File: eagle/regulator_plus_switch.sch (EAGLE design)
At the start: 67 parts, among them IC2 LT1352PA, IC3 DG419DJN, IC4 LT1352PA, Q1 2N3906, Q2 2N3906, T1 2N3904, T2 2N3904

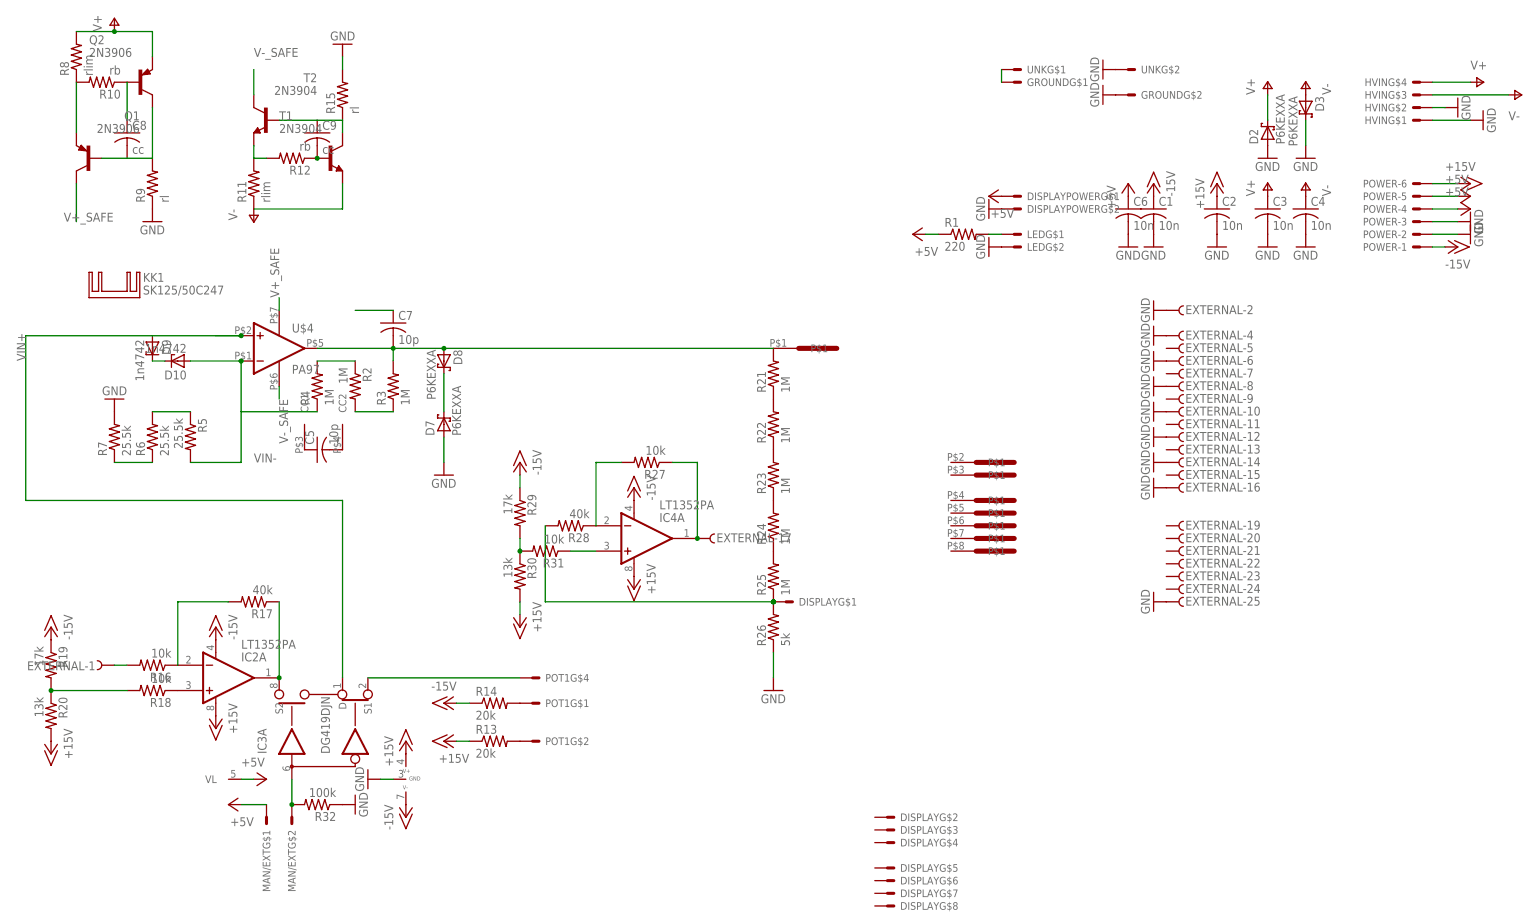
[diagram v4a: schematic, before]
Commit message: overcurrent, worked out connectors
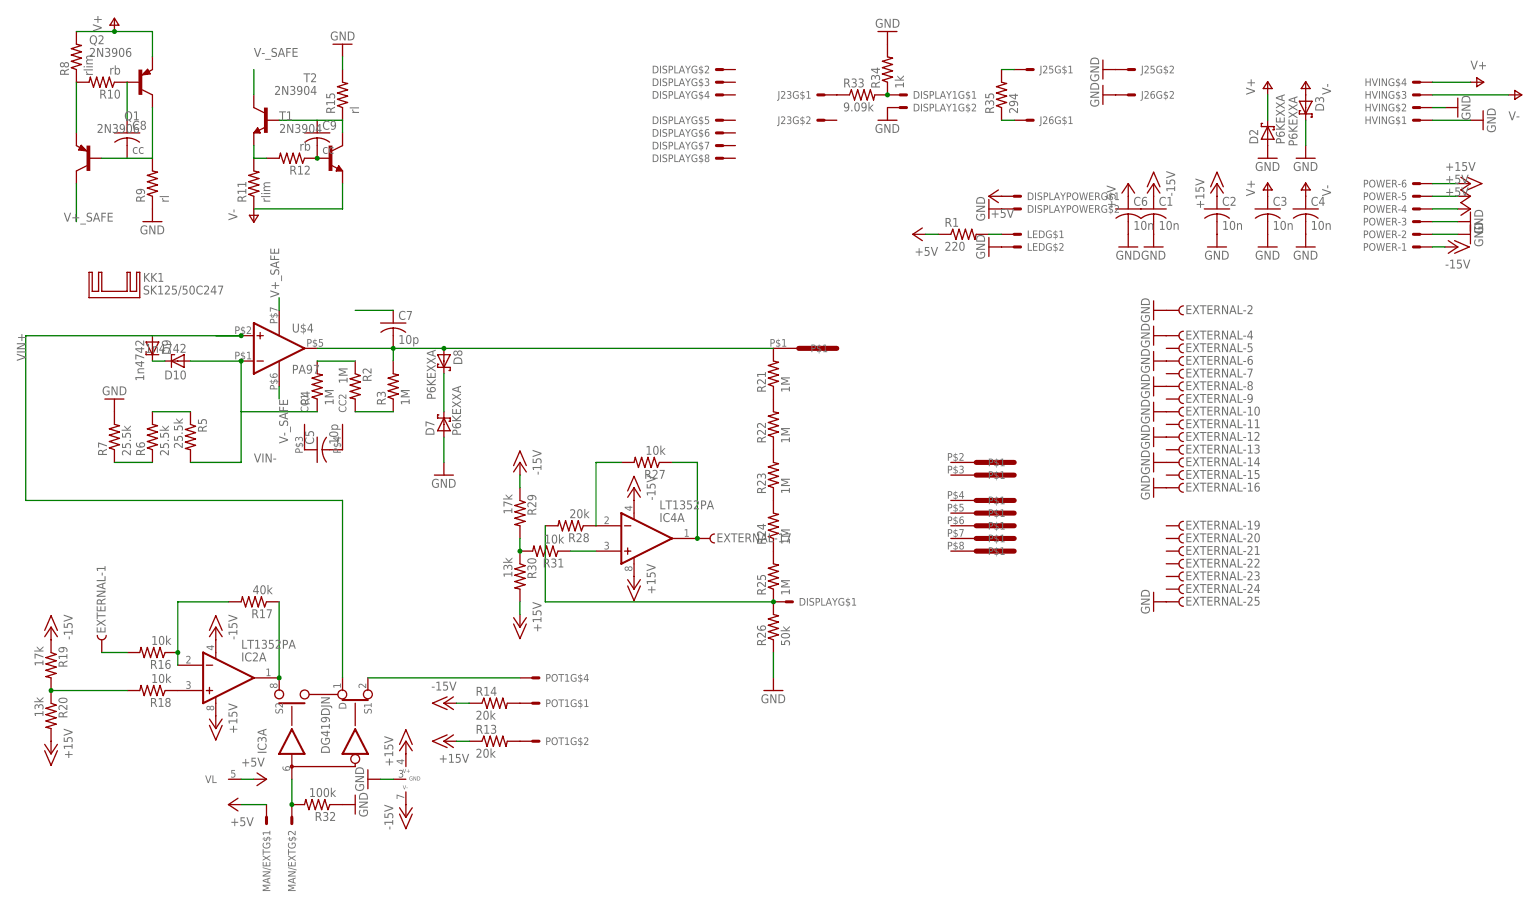
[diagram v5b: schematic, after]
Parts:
- removed GROUND, UNK: 5569-2, con-molex:5569-2
- added DISPLAY1, J23, J25, J26: 5569-2, con-molex:5569-2
- added R33: 9.09k, rcl:R-US_0207/10
- added R34: 1k, rcl:R-US_0207/10
- added R35: 294, rcl:R-US_0207/10
- R26: value 5k -> 50k
- R28: value 40k -> 20k
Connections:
- new net N$20: DISPLAY1G$1.S, R33.2, R34.1
- new net N$21: J23G$1.S, R33.1
- new net N$22: J26G$1.S, R35.1
- net GND: now also DISPLAY1G$2.S, J25G$2.S, J26G$2.S, R34.2; no longer GROUNDG$2.S, UNKG$2.S
- net N$6: now also J25G$1.S, R35.2; no longer GROUNDG$1.S, UNKG$1.S
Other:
- moved on the sheet: DISPLAYG$1, DISPLAYG$2, DISPLAYG$3, DISPLAYG$4, DISPLAYG$5, DISPLAYG$6, DISPLAYG$7, DISPLAYG$8, EXTERNAL-1, R16
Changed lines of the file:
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@@
 <part name="R24" library="resistor" deviceset="R-US_" device="0207/10" value="1M"/>
 <part name="R25" library="resistor" deviceset="R-US_" device="0207/10" value="1M"/>
-<part name="R26" library="rcl" deviceset="R-US_" device="0207/10" value="5k"/>
+<part name="R26" library="rcl" deviceset="R-US_" device="0207/10" value="50k"/>
 <part name="GND24" library="supply1" deviceset="GND" device=""/>
 <part name="IC4" library="linear-technology" deviceset="LT1352" device="PA"/>
@@
 <part name="P+16" library="supply1" deviceset="+15V" device=""/>
 <part name="R27" library="rcl" deviceset="R-US_" device="0207/10" value="10k"/>
-<part name="R28" library="rcl" deviceset="R-US_" device="0207/10" value="40k"/>
+<part name="R28" library="rcl" deviceset="R-US_" device="0207/10" value="20k"/>
 <part name="R29" library="rcl" deviceset="R-US_" device="0207/10" value="17k"/>
 <part name="R30" library="rcl" deviceset="R-US_" device="0207/10" value="13k"/>
@@
 <part name="OUT" library="con-amp-te" deviceset="640584-1" device=""/>
 <part name="DISPLAY" library="con-molex" deviceset="5669-8" device=""/>
-<part name="UNK" library="con-molex" deviceset="5569-2" device=""/>
-<part name="GROUND" library="con-molex" deviceset="5569-2" device=""/>
+<part name="J25" library="con-molex" deviceset="5569-2" device=""/>
+<part name="J26" library="con-molex" deviceset="5569-2" device=""/>
 <part name="DISPLAYPOWER" library="con-molex" deviceset="5569-2" device=""/>
 <part name="LED" library="con-molex" deviceset="5569-2" device=""/>
@@
 <part name="R15" library="rcl" deviceset="R-US_" device="0207/10" value="rl"/>
 <part name="GND31" library="supply1" deviceset="GND" device=""/>
+<part name="DISPLAY1" library="con-molex" deviceset="5569-2" device=""/>
+<part name="R33" library="rcl" deviceset="R-US_" device="0207/10" value="9.09k"/>
+<part name="R34" library="rcl" deviceset="R-US_" device="0207/10" value="1k"/>
+<part name="GND32" library="supply1" deviceset="GND" device=""/>
+<part name="GND33" library="supply1" deviceset="GND" device=""/>
+<part name="J23" library="con-molex" deviceset="5569-2" device=""/>
+<part name="R35" library="rcl" deviceset="R-US_" device="0207/10" value="294"/>
 </parts>
 <sheets>
@@
 <instance part="HVIN" gate="G$4" x="294.64" y="840.74" rot="R180"/>
 <instance part="IC2" gate="A" x="55.88" y="721.36" rot="MR180"/>
-<instance part="R16" gate="G$1" x="40.64" y="723.9" rot="R180"/>
+<instance part="R16" gate="G$1" x="40.64" y="726.44" rot="R180"/>
 <instance part="R17" gate="G$1" x="60.96" y="736.6" rot="R180"/>
 <instance part="R18" gate="G$1" x="40.64" y="718.82" rot="R180"/>
@@
 <instance part="P-5" gate="1" x="91.44" y="693.42"/>
 <instance part="GND12" gate="1" x="83.82" y="701.04" rot="R270"/>
-<instance part="EXTERNAL" gate="-1" x="30.48" y="723.9" rot="R180"/>
+<instance part="EXTERNAL" gate="-1" x="30.48" y="728.98" rot="R90"/>
 <instance part="EXTERNAL" gate="-2" x="246.38" y="795.02"/>
 <instance part="EXTERNAL" gate="-4" x="246.38" y="789.94"/>
@@
 <instance part="OUT" gate="G$7" x="205.74" y="749.3"/>
 <instance part="OUT" gate="G$8" x="205.74" y="746.76"/>
-<instance part="DISPLAY" gate="G$1" x="167.64" y="736.6"/>
-<instance part="DISPLAY" gate="G$2" x="187.96" y="693.42"/>
-<instance part="DISPLAY" gate="G$3" x="187.96" y="690.88"/>
-<instance part="DISPLAY" gate="G$4" x="187.96" y="688.34"/>
-<instance part="DISPLAY" gate="G$5" x="187.96" y="683.26"/>
-<instance part="DISPLAY" gate="G$6" x="187.96" y="680.72"/>
-<instance part="DISPLAY" gate="G$7" x="187.96" y="678.18"/>
-<instance part="DISPLAY" gate="G$8" x="187.96" y="675.64"/>
-<instance part="UNK" gate="G$1" x="213.36" y="843.28"/>
-<instance part="UNK" gate="G$2" x="236.22" y="843.28"/>
-<instance part="GROUND" gate="G$1" x="213.36" y="840.74"/>
-<instance part="GROUND" gate="G$2" x="236.22" y="838.2"/>
+<instance part="DISPLAY" gate="G$1" x="167.64" y="736.6" rot="MR180"/>
+<instance part="DISPLAY" gate="G$2" x="154.94" y="843.28" rot="MR0"/>
+<instance part="DISPLAY" gate="G$3" x="154.94" y="840.74" rot="MR0"/>
+<instance part="DISPLAY" gate="G$4" x="154.94" y="838.2" rot="MR0"/>
+<instance part="DISPLAY" gate="G$5" x="154.94" y="833.12" rot="MR0"/>
+<instance part="DISPLAY" gate="G$6" x="154.94" y="830.58" rot="MR0"/>
+<instance part="DISPLAY" gate="G$7" x="154.94" y="828.04" rot="MR0"/>
+<instance part="DISPLAY" gate="G$8" x="154.94" y="825.5" rot="MR0"/>
+<instance part="J25" gate="G$1" x="215.9" y="843.28"/>
+<instance part="J25" gate="G$2" x="236.22" y="843.28"/>
+<instance part="J26" gate="G$1" x="215.9" y="833.12"/>
+<instance part="J26" gate="G$2" x="236.22" y="838.2"/>
 <instance part="DISPLAYPOWER" gate="G$1" x="213.36" y="817.88"/>
 <instance part="DISPLAYPOWER" gate="G$2" x="213.36" y="815.34"/>
@@
 <instance part="R15" gate="G$1" x="78.74" y="838.2" rot="R90"/>
 <instance part="GND31" gate="1" x="78.74" y="848.36" rot="R180"/>
+<instance part="DISPLAY1" gate="G$1" x="190.5" y="838.2"/>
+<instance part="DISPLAY1" gate="G$2" x="190.5" y="835.66"/>
+<instance part="R33" gate="G$1" x="182.88" y="838.2"/>
+<instance part="R34" gate="G$1" x="187.96" y="843.28" rot="R90"/>
+<instance part="GND32" gate="1" x="187.96" y="850.9" rot="R180"/>
+<instance part="GND33" gate="1" x="187.96" y="833.12"/>
+<instance part="J23" gate="G$1" x="175.26" y="838.2" rot="R180"/>
+<instance part="J23" gate="G$2" x="175.26" y="833.12" rot="R180"/>
+<instance part="R35" gate="G$1" x="210.82" y="838.2" rot="R90"/>
 </instances>
 <busses>
@@
 </segment>
 <segment>
-<pinref part="UNK" gate="G$2" pin="S"/>
+<pinref part="J25" gate="G$2" pin="S"/>
 <pinref part="GND7" gate="1" pin="GND"/>
 </segment>
 <segment>
-<pinref part="GROUND" gate="G$2" pin="S"/>
+<pinref part="J26" gate="G$2" pin="S"/>
 <pinref part="GND8" gate="1" pin="GND"/>
 </segment>
@@
 <pinref part="GND31" gate="1" pin="GND"/>
 <wire x1="78.74" y1="843.28" x2="78.74" y2="845.82" width="0.1524" layer="91"/>
+</segment>
+<segment>
+<pinref part="R34" gate="G$1" pin="2"/>
+<pinref part="GND32" gate="1" pin="GND"/>
+</segment>
+<segment>
+<pinref part="DISPLAY1" gate="G$2" pin="S"/>
+<pinref part="GND33" gate="1" pin="GND"/>
 </segment>
 </net>
@@
 <pinref part="R17" gate="G$1" pin="2"/>
 <wire x1="55.88" y1="736.6" x2="45.72" y2="736.6" width="0.1524" layer="91"/>
-<wire x1="45.72" y1="736.6" x2="45.72" y2="723.9" width="0.1524" layer="91"/>
+<wire x1="45.72" y1="736.6" x2="45.72" y2="726.44" width="0.1524" layer="91"/>
+<wire x1="45.72" y1="726.44" x2="45.72" y2="723.9" width="0.1524" layer="91"/>
+<junction x="45.72" y="726.44"/>
 </segment>
 </net>
@@
 <pinref part="R16" gate="G$1" pin="2"/>
 <pinref part="EXTERNAL" gate="-1" pin="F"/>
-<wire x1="33.02" y1="723.9" x2="35.56" y2="723.9" width="0.1524" layer="91"/>
+<wire x1="30.48" y1="726.44" x2="35.56" y2="726.44" width="0.1524" layer="91"/>
 </segment>
 </net>
@@
 <wire x1="165.1" y1="736.6" x2="119.38" y2="736.6" width="0.1524" layer="91"/>
 <wire x1="119.38" y1="736.6" x2="119.38" y2="751.84" width="0.1524" layer="91"/>
+<junction x="165.1" y="736.6"/>
 <pinref part="DISPLAY" gate="G$1" pin="S"/>
-<junction x="165.1" y="736.6"/>
-<junction x="165.1" y="736.6"/>
-<junction x="165.1" y="736.6"/>
 </segment>
 </net>
@@
 <net name="N$6" class="0">
 <segment>
-<pinref part="UNK" gate="G$1" pin="S"/>
-<pinref part="GROUND" gate="G$1" pin="S"/>
-<wire x1="210.82" y1="843.28" x2="210.82" y2="840.74" width="0.1524" layer="91"/>
+<pinref part="J25" gate="G$1" pin="S"/>
+<pinref part="R35" gate="G$1" pin="2"/>
+<wire x1="213.36" y1="843.28" x2="210.82" y2="843.28" width="0.1524" layer="91"/>
 </segment>
 </net>
@@
 </segment>
 </net>
+<net name="N$20" class="0">
+<segment>
+<pinref part="DISPLAY1" gate="G$1" pin="S"/>
+<pinref part="R33" gate="G$1" pin="2"/>
+<pinref part="R34" gate="G$1" pin="1"/>
+<pinref part="R34" gate="G$1" pin="1"/>
+<junction x="187.96" y="838.2"/>
+</segment>
+</net>
+<net name="N$21" class="0">
+<segment>
+<pinref part="R33" gate="G$1" pin="1"/>
+<pinref part="J23" gate="G$1" pin="S"/>
+</segment>
+</net>
+<net name="N$22" class="0">
+<segment>
+<pinref part="J26" gate="G$1" pin="S"/>
+<pinref part="R35" gate="G$1" pin="1"/>
+<wire x1="213.36" y1="833.12" x2="210.82" y2="833.12" width="0.1524" layer="91"/>
+</segment>
+</net>

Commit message: yay led switch worked out
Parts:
- removed DISPLAYPOWER, J25, LED: 5569-2, con-molex:5569-2
- removed R1: 220, rcl:R-US_0207/10
- added DISPLAYPOWERJ25: 5569-2, con-molex:5569-2
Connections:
- removed net N$6: J25G$1.S, R35.2
- removed net N$7: LEDG$1.S, R1.2
- net +5V: now also DISPLAYPOWERJ25G$1.S, R35.2; no longer DISPLAYPOWERG$1.S, R1.1
- net GND: now also DISPLAYPOWERJ25G$2.S; no longer DISPLAYPOWERG$2.S, J25G$2.S, LEDG$2.S
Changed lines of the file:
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@@
 <part name="OUT" library="con-amp-te" deviceset="640584-1" device=""/>
 <part name="DISPLAY" library="con-molex" deviceset="5669-8" device=""/>
-<part name="J25" library="con-molex" deviceset="5569-2" device=""/>
 <part name="J26" library="con-molex" deviceset="5569-2" device=""/>
-<part name="DISPLAYPOWER" library="con-molex" deviceset="5569-2" device=""/>
-<part name="LED" library="con-molex" deviceset="5569-2" device=""/>
+<part name="DISPLAYPOWERJ25" library="con-molex" deviceset="5569-2" device=""/>
 <part name="P+3" library="supply1" deviceset="+5V" device=""/>
 <part name="GND5" library="supply1" deviceset="GND" device=""/>
-<part name="GND7" library="supply1" deviceset="GND" device=""/>
 <part name="GND8" library="supply1" deviceset="GND" device=""/>
-<part name="P+4" library="supply1" deviceset="+5V" device=""/>
-<part name="R1" library="rcl" deviceset="R-US_" device="0207/10" value="220"/>
-<part name="GND14" library="supply1" deviceset="GND" device=""/>
 <part name="P+5" library="supply1" deviceset="V+" device=""/>
 <part name="P-3" library="supply1" deviceset="V-" device=""/>
@@
 <part name="J23" library="con-molex" deviceset="5569-2" device=""/>
 <part name="R35" library="rcl" deviceset="R-US_" device="0207/10" value="294"/>
+<part name="P+14" library="supply1" deviceset="+5V" device=""/>
 </parts>
 <sheets>
@@
 <instance part="DISPLAY" gate="G$7" x="154.94" y="828.04" rot="MR0"/>
 <instance part="DISPLAY" gate="G$8" x="154.94" y="825.5" rot="MR0"/>
-<instance part="J25" gate="G$1" x="215.9" y="843.28"/>
-<instance part="J25" gate="G$2" x="236.22" y="843.28"/>
 <instance part="J26" gate="G$1" x="215.9" y="833.12"/>
 <instance part="J26" gate="G$2" x="236.22" y="838.2"/>
-<instance part="DISPLAYPOWER" gate="G$1" x="213.36" y="817.88"/>
-<instance part="DISPLAYPOWER" gate="G$2" x="213.36" y="815.34"/>
-<instance part="LED" gate="G$1" x="213.36" y="810.26"/>
-<instance part="LED" gate="G$2" x="213.36" y="807.72"/>
-<instance part="P+3" gate="1" x="208.28" y="817.88" rot="R90"/>
-<instance part="GND5" gate="1" x="208.28" y="815.34" rot="R270"/>
-<instance part="GND7" gate="1" x="231.14" y="843.28" rot="R270"/>
+<instance part="DISPLAYPOWERJ25" gate="G$1" x="185.42" y="822.96"/>
+<instance part="DISPLAYPOWERJ25" gate="G$2" x="185.42" y="820.42"/>
+<instance part="P+3" gate="1" x="180.34" y="822.96" rot="R90"/>
+<instance part="GND5" gate="1" x="180.34" y="820.42" rot="R270"/>
 <instance part="GND8" gate="1" x="231.14" y="838.2" rot="R270"/>
-<instance part="P+4" gate="1" x="193.04" y="810.26" rot="R90"/>
-<instance part="R1" gate="G$1" x="203.2" y="810.26"/>
-<instance part="GND14" gate="1" x="208.28" y="807.72" rot="R270"/>
 <instance part="P+5" gate="1" x="264.16" y="840.74"/>
 <instance part="P-3" gate="1" x="271.78" y="840.74" rot="R180"/>
@@
 <instance part="J23" gate="G$2" x="175.26" y="833.12" rot="R180"/>
 <instance part="R35" gate="G$1" x="210.82" y="838.2" rot="R90"/>
+<instance part="P+14" gate="1" x="213.36" y="843.28" rot="R270"/>
 </instances>
 <busses>
@@
 </segment>
 <segment>
-<pinref part="DISPLAYPOWER" gate="G$2" pin="S"/>
+<pinref part="DISPLAYPOWERJ25" gate="G$2" pin="S"/>
 <pinref part="GND5" gate="1" pin="GND"/>
-</segment>
-<segment>
-<pinref part="J25" gate="G$2" pin="S"/>
-<pinref part="GND7" gate="1" pin="GND"/>
 </segment>
 <segment>
 <pinref part="J26" gate="G$2" pin="S"/>
 <pinref part="GND8" gate="1" pin="GND"/>
-</segment>
-<segment>
-<pinref part="LED" gate="G$2" pin="S"/>
-<pinref part="GND14" gate="1" pin="GND"/>
 </segment>
 <segment>
@@
 </segment>
 <segment>
-<pinref part="DISPLAYPOWER" gate="G$1" pin="S"/>
+<pinref part="DISPLAYPOWERJ25" gate="G$1" pin="S"/>
 <pinref part="P+3" gate="1" pin="+5V"/>
-</segment>
-<segment>
-<pinref part="P+4" gate="1" pin="+5V"/>
-<pinref part="R1" gate="G$1" pin="1"/>
-<wire x1="195.58" y1="810.26" x2="198.12" y2="810.26" width="0.1524" layer="91"/>
 </segment>
 <segment>
 <pinref part="P+19" gate="1" pin="+5V"/>
 <pinref part="C6" gate="G$1" pin="1"/>
+</segment>
+<segment>
+<pinref part="R35" gate="G$1" pin="2"/>
+<pinref part="P+14" gate="1" pin="+5V"/>
 </segment>
 </net>
@@
 </segment>
 </net>
-<net name="N$6" class="0">
-<segment>
-<pinref part="J25" gate="G$1" pin="S"/>
-<pinref part="R35" gate="G$1" pin="2"/>
-<wire x1="213.36" y1="843.28" x2="210.82" y2="843.28" width="0.1524" layer="91"/>
-</segment>
-</net>
-<net name="N$7" class="0">
-<segment>
-<pinref part="LED" gate="G$1" pin="S"/>
-<pinref part="R1" gate="G$1" pin="2"/>
-<wire x1="208.28" y1="810.26" x2="210.82" y2="810.26" width="0.1524" layer="91"/>
-</segment>
-</net>
